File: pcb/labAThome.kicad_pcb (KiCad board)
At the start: 2 copper layers, 100 x 100 mm, 57 parts, among them J1 BME280, J10 SRV2, J12 FA2, J13 Barrel_Jack_Switch, J14 FA3, J2 SRV1, J3 5V, J4 EXTENSION, J5 VPS, J9 FA1, K1 G5V-2, K2 G5V-2, K3 G5V-2, Q2 IRLZ44N, Q3 IRLZ44N, Q4 BC547, SW1 RED, SW2 GREEN, SW3 YELLOW, SW4 BLUE, SW5 WHITE, SW6 FAN, U1 HC-SR501, U2 24V->5V, U3 PDC004_Module, U4 ESP32_DEVKITC_COMPATIBLE, U5 LD06AJSA, U6 GY-302, U7 Display, U8 INMP441_Module

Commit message: SchematicsV3 as ordered at JLCPCB
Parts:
- removed D1: RED, LED_THT:LED_D5.0mm
- removed D2: GREEN, LED_THT:LED_D5.0mm
- removed D3: YELLOW, LED_THT:LED_D5.0mm
- removed J14: FA3, Connector:FanPinHeader_1x03_P2.54mm_Vertical
- added C1: CP, Capacitor_THT:CP_Radial_Tantal_D5.0mm_P5.00mm, F.Cu at (72.1, 61.7)
- added D5: 1N4001, Diode_THT:D_DO-41_SOD81_P7.62mm_Horizontal, B.Cu at (73.7, 64.5)
- added J11: 1wire, Connector_JST:JST_PH_B3B-PH-K_1x03_P2.00mm_Vertical, B.Cu at (41.7, 101.2)
- added J6: FAN3, Connector:FanPinHeader_1x03_P2.54mm_Vertical, B.Cu at (48.5, 64.5)
- added J7: 1wire, Connector_JST:JST_PH_B3B-PH-K_1x03_P2.00mm_Vertical, B.Cu at (41.6, 87.1)
- added J8: 1wire, Connector_JST:JST_PH_B3B-PH-K_1x03_P2.00mm_Vertical, B.Cu at (47.4, 81.4)
- added JP4: 5V FAN1+2 24V, Connector_PinSocket_2.54mm:PinSocket_1x03_P2.54mm_Vertical, F.Cu at (43.3, 60.2)
- added Q1: IRLZ44N, Package_TO_SOT_THT:TO-220-3_Horizontal_TabDown, B.Cu at (58.3, 90.8)
- added U10: MAX3485_MODULE, smopla:MAX3485_MODULE, B.Cu at (99.1, 116.3)
- added U11: AM312, smopla:AM312, F.Cu at (80.0, 59.6)
- added U9: NEOPIXEL_STICK, smopla:NEOPIXEL_STICK, F.Cu at (47.9, 38.5)
- added X1: FAN_6024, smopla:FAN_6024, B.Cu at (74.5, 110.2)
- BZ1: footprint Buzzer_Beeper:Buzzer_12x9.5RM7.6 -> smopla:Buzzer_12x9.5RM6.6
- D8: footprint Diode_THT:D_DO-35_SOD27_P7.62mm_Horizontal -> Diode_THT:D_DO-35_SOD27_P2.54mm_Vertical_AnodeUp
- J1: footprint Connector_PinHeader_2.54mm:PinHeader_1x06_P2.54mm_Vertical -> Connector_PinHeader_2.54mm:PinHeader_1x04_P2.54mm_Vertical; moved to F.Cu
- J12: value FA2 -> FAN2
- J3: footprint Connector_PinHeader_2.54mm:PinHeader_1x05_P2.54mm_Vertical -> Connector_PinHeader_2.54mm:PinHeader_1x04_P2.54mm_Vertical
- J9: value FA1 -> FAN1
- JP3: value 3V3_5V -> R3_BUZZ; footprint Jumper:SolderJumper-3_P2.0mm_Open_TrianglePad1.0x1.5mm_NumberLabels -> Connector_PinSocket_2.54mm:PinSocket_1x03_P2.54mm_Vertical
- Q4: footprint Package_TO_SOT_THT:TO-92_Inline -> Package_TO_SOT_THT:TO-92_HandSolder
- R1, R13, R14, R15, R16, R2, R6: footprint Resistor_THT:R_Axial_DIN0207_L6.3mm_D2.5mm_P7.62mm_Horizontal -> Resistor_THT:R_Axial_DIN0207_L6.3mm_D2.5mm_P2.54mm_Vertical
- R3, R5: value 68R -> 1K; footprint Resistor_THT:R_Axial_DIN0207_L6.3mm_D2.5mm_P7.62mm_Horizontal -> Resistor_THT:R_Axial_DIN0207_L6.3mm_D2.5mm_P2.54mm_Vertical
- R4: value 68R -> 10K; footprint Resistor_THT:R_Axial_DIN0207_L6.3mm_D2.5mm_P7.62mm_Horizontal -> Resistor_THT:R_Axial_DIN0207_L6.3mm_D2.5mm_P2.54mm_Vertical
- SW6: value FAN -> FAN2; footprint smopla:MTS-102 -> smopla:SS12D00
- U1: value HC-SR501 -> SR602; footprint smopla:HC-SR501 -> smopla:SR602
- moved R1 68.4 mm to (47.5, 86.9), turned to 90 degrees
- moved JP3 46.0 mm to (96.5, 103.4)
- moved R2 45.8 mm to (50.5, 86.9)
- moved R10 34.9 mm to (118.6, 60.5), turned to 180 degrees
- moved U5 34.2 mm to (50.8, 112.4), turned to 180 degrees
- moved R14 21.2 mm to (123.7, 124.7), turned to 180 degrees
- moved R12 20.4 mm to (91.9, 81.5), turned to 90 degrees
- moved Q4 18.7 mm to (95.5, 78.5)
- moved R5 18.3 mm to (47.4, 76.6), turned to 0 degrees
- moved R3 14.2 mm to (50.5, 92.2), turned to 90 degrees
- moved RV1 13.4 mm to (39.6, 70.0)
- moved R15 12.2 mm to (50.4, 106.4)
- moved R16 12.2 mm to (47.4, 106.4)
- moved J12 8.84 mm to (34.7, 65.3)
- moved R13 8.66 mm to (103.1, 110.5), turned to 180 degrees
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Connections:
- J10 pad 1: I2S_SD -> 1wire
- J2 pad 1: I2S_SCK -> SERVO_PWM1
- J9 pad 2: +5V -> Net-(J6-Pad2)
- JP3 pad 1: +3V3 -> R3_ON
- JP3 pad 3: +5V -> BUZZER
- R11 pad 1: /Q2_D -> +24V
- R11 pad 2: +24V -> /Q2_D
- R3 pad 1: +3V3 -> 1wire
- R3 pad 2: Net-(D1-Pad2) -> Net-(Q1-Pad1)
- R4 pad 1: +3V3 -> GND
- R4 pad 2: Net-(D2-Pad2) -> Net-(Q1-Pad1)
- R5 pad 2: Net-(D3-Pad2) -> 1wire
- U1 pad 1: Net-(JP3-Pad2) -> +3V3
- U1 pad 2: MOVEMENT -> GND
- U1 pad 3: GND -> MOVEMENT
- U4 pad 10: LED_RED -> LED_STRIP
- U4 pad 11: LED_YELLOW -> 1wire
- U4 pad 12: LED_POWER_WHITE -> I2S_SCK
- U4 pad 15: LED_GREEN -> LED_POWER_WHITE
- U4 pad 24: LCD_BL -> HEATER
- U4 pad 26: I2S_SD -> I2S_WS
- U4 pad 27: HEATER -> I2S_SD
- U4 pad 28: R3_ON -> Net-(JP3-Pad2)
- U4 pad 29: BUZZER -> LCD_DC
- U4 pad 31: LCD_DC -> LCD_RES
- U4 pad 9: I2S_SCK -> SERVO_PWM1
- U7 pad 5: +3V3 -> LCD_RES
- U7 pad 7: LCD_BL -> Net-(U7-Pad7)
- U8 pad 2: HEATER -> I2S_WS
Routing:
- net Net-(J5-Pad1): track 6.22 -> 108.9 mm, vias 0 -> 3
- net LED_STRIP: track 0.00 -> 94.1 mm
- net I2S_SD: track 113.4 -> 19.6 mm, vias 1 -> 0
- net 1wire: track 0.00 -> 93.6 mm, vias 0 -> 1
- net R3_A1: track 74.1 -> 9.43 mm, vias 1 -> 0
- net LED_POWER_WHITE: track 61.3 -> 4.07 mm, vias 1 -> 0
- net SERVO_PWM1: track 0.00 -> 55.0 mm
- net I2S_SCK: track 103.1 -> 48.3 mm, vias 1 -> 7
- net GND: track 89.4 -> 142.1 mm, vias 19 -> 201
- net LCD_BL: track 43.9 -> 0.00 mm
- net Net-(D5-Pad1): track 0.00 -> 37.2 mm
- net R3_12: track 42.5 -> 12.6 mm
- net /FAN_SWITCH2: track 0.00 -> 27.8 mm
- net I2S_WS: track 0.00 -> 25.2 mm
- net Net-(D2-Pad2): track 22.6 -> 0.00 mm
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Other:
- board text added: "-"
- board text added: "EXT"
- board text added: "Gegenseitiger Ausschluss: - 1wire und Servo2 - I2S und RS485 - Relay 3 und Buzzer"
- board text removed: "EXTENSION CONNECTOR"

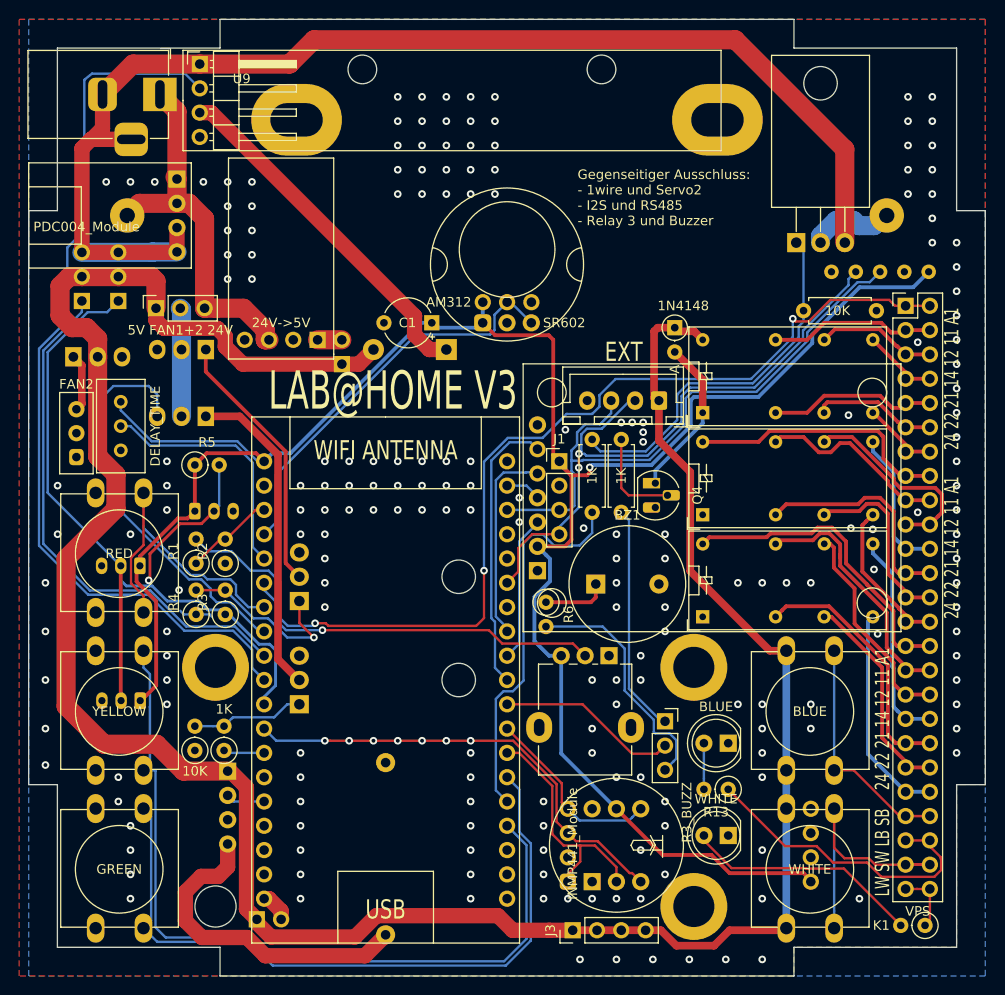
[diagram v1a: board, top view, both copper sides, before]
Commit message: PCB  V4 as ordered at JLCPCB
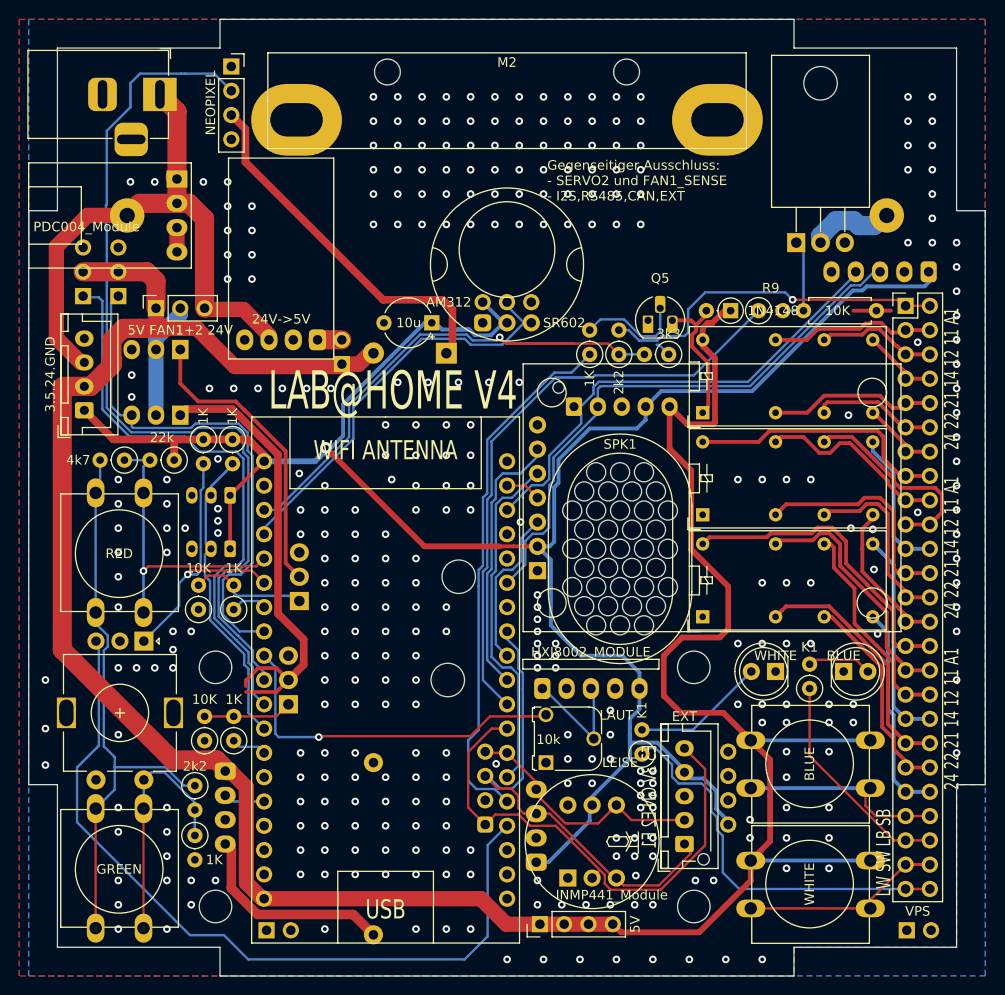
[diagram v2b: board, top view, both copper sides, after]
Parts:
- removed BZ1: Buzzer, smopla:Buzzer_12x9.5RM6.6
- removed Q4: BC547, Package_TO_SOT_THT:TO-92_HandSolder
- removed R6: K1, Resistor_THT:R_Axial_DIN0207_L6.3mm_D2.5mm_P2.54mm_Vertical
- removed RV2: R_POT, Potentiometer_THT:Potentiometer_Alpha_RD901F-40-00D_Single_Vertical
- removed SW3: YELLOW, Button_Switch_THT:SW_PUSH-12mm
- removed SW6: FAN2, smopla:SS12D00
- removed U9: NEOPIXEL_STICK, smopla:NEOPIXEL_STICK
- added M1: HXJ8002_MODULE, smopla:HXJ8002_MODULE_VERTICAL, F.Cu at (83.7, 99.9)
- added M2: NEOPIXEL, smopla:NEOPIXEL_STICK, F.Cu at (80.0, 35.5)
- added M3: SN65HVD230_MODULE, smopla:SN65HVD230_MODULE, B.Cu at (83.1, 114.3)
- added Q5: 2N3904, Package_TO_SOT_THT:TO-92_HandSolder, F.Cu at (94.7, 61.5)
- added R18: 22k, Resistor_THT:R_Axial_DIN0207_L6.3mm_D2.5mm_P2.54mm_Vertical, F.Cu at (45.2, 76.1)
- added R19: 4k7, Resistor_THT:R_Axial_DIN0207_L6.3mm_D2.5mm_P2.54mm_Vertical, F.Cu at (40.0, 76.1)
- added R20: 2k2, Resistor_THT:R_Axial_DIN0207_L6.3mm_D2.5mm_P2.54mm_Vertical, F.Cu at (47.4, 110.1)
- added R21: 1K, Resistor_THT:R_Axial_DIN0207_L6.3mm_D2.5mm_P2.54mm_Vertical, F.Cu at (47.4, 115.3)
- added R7: 1K, Resistor_THT:R_Axial_DIN0207_L6.3mm_D2.5mm_P2.54mm_Vertical, F.Cu at (48.3, 73.9)
- added SPK1: SPEAKER, smopla:SPEAKER_2415, F.Cu at (91.8, 85.3)
- added SW7: ROTENC, smopla:RotaryEncoder_Alps_EC11E-Switch_Vertical_H20mm, F.Cu at (42.0, 95.0)
- C1: value CP -> 10u
- J1: value BME280 -> I2C; footprint Connector_PinHeader_2.54mm:PinHeader_1x04_P2.54mm_Vertical -> Connector_JST:JST_XH_B5B-XH-AM_1x05_P2.50mm_Vertical; moved to B.Cu
- J11: value 1wire -> 3.5.24.GND; footprint Connector_JST:JST_PH_B3B-PH-K_1x03_P2.00mm_Vertical -> Connector_JST:JST_XH_B4B-XH-A_1x04_P2.50mm_Vertical; moved to F.Cu
- J12: value FAN2 -> NEOPIXEL; footprint Connector:FanPinHeader_1x03_P2.54mm_Vertical -> Connector_PinSocket_2.54mm:PinSocket_1x04_P2.54mm_Vertical; moved to F.Cu
- J4: value EXTENSION -> EXT; footprint Connector_JST:JST_XH_B4B-XH-A_1x04_P2.50mm_Vertical -> Connector_JST:JST_XH_B5B-XH-AM_1x05_P2.50mm_Vertical
- JP2: value 5V_ESP -> MECHANICAL
- JP3: value R3_BUZZ -> MECHANICAL; footprint Connector_PinSocket_2.54mm:PinSocket_1x03_P2.54mm_Vertical -> Connector_PinHeader_2.54mm:PinHeader_1x02_P2.54mm_Vertical; moved to B.Cu
- R12, R9: footprint Resistor_THT:R_Axial_DIN0207_L6.3mm_D2.5mm_P7.62mm_Horizontal -> Resistor_THT:R_Axial_DIN0207_L6.3mm_D2.5mm_P2.54mm_Vertical
- RV1: value DELAY_TIME -> 10k; footprint Potentiometer_THT:Potentiometer_Bourns_3296W_Vertical -> Potentiometer_THT:Potentiometer_Runtron_RM-065_Vertical
- moved RV1 58.3 mm to (84.1, 107.7)
- moved R2 51.2 mm to (96.9, 65.0), turned to 180 degrees
- moved R1 49.3 mm to (91.7, 65.0)
- moved J4 46.4 mm to (98.6, 116.2), turned to 90 degrees
- moved R14 34.6 mm to (94.1, 106.8), turned to 90 degrees
- moved J12 34.6 mm to (51.2, 34.9)
- moved JP3 33.4 mm to (121.8, 125.2), turned to 270 degrees
- moved J11 30.9 mm to (35.8, 70.9), turned to 90 degrees
- moved R9 27.3 mm to (106.3, 60.5), turned to 0 degrees
- moved D7 17.8 mm to (108.1, 98.2)
- moved R12 16.8 mm to (88.6, 65.0)
- moved SW4 14.9 mm to (118.0, 110.4), turned to 180 degrees
- moved D6 14.2 mm to (115.2, 98.2), turned to 0 degrees
- moved R13 13.5 mm to (111.6, 99.9), turned to 90 degrees
- moved SW5 11.1 mm to (118.0, 122.9), turned to 180 degrees
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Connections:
- net FAN_DRIVE renamed FAN1_DRIVE
- net Net-(J5-Pad1) renamed /R3_INPUT
- J1 pad 1: +3V3 -> SDA
- J1 pad 2: GND -> SCL
- J1 pad 3: SCL -> GND
- J1 pad 4: SDA -> +3V3
- J10 pad 1: 1wire -> FAN1_SENSE
- J11 pad 2: 1wire -> +5V
- J11 pad 3: GND -> +24V
- J12 pad 1: Net-(J12-Pad1) -> GND
- J12 pad 2: +5V -> LED_STRIP
- J12 pad 3: Net-(J12-Pad3) -> Net-(D5-Pad1)
- J2 pad 1: SERVO_PWM1 -> SERVO1
- J4 pad 1: +5V -> 485_DE
- J4 pad 2: SDA -> 485_DI
- J4 pad 3: SCL -> GND
- J4 pad 4: GND -> +3V3
- J9 pad 3: FAN_SENSE -> FAN1_SENSE
- JP2 pad 1: +5V -> GND
- JP2 pad 2: Net-(JP2-Pad2) -> GND
- JP3 pad 1: R3_ON -> GND
- JP3 pad 2: Net-(JP3-Pad2) -> GND
- R3 pad 1: 1wire -> FAN2_DRIVE
- RV1 pad 1: +3V3 -> GND
- RV1 pad 2: POTI_T -> Net-(M1-Pad1)
- RV1 pad 3: GND -> SPEAKER
- SW1 pad 1: SW_RED -> SW
- SW1 pad 2: GND -> Net-(R19-Pad2)
- SW2 pad 1: SW_GREEN -> Net-(R20-Pad2)
- SW2 pad 2: GND -> Net-(R19-Pad2)
- U1 pad 1: +3V3 -> GND
- U1 pad 2: GND -> +3V3
- U10 pad 1: I2S_WS -> 485_RO
- U10 pad 3: I2S_SCK -> 485_DE
- U10 pad 4: I2S_SD -> 485_DI
- U4 pad 11: 1wire -> SERVO1
- U4 pad 12: I2S_SCK -> 1wire
- U4 pad 19: Net-(JP2-Pad2) -> +5V
- U4 pad 23: SW_YELLOW -> ROTENC_B
- U4 pad 24: HEATER -> R3_ON
- U4 pad 25: SW_GREEN -> LCD_RES
- U4 pad 26: I2S_WS -> 485_DI
- U4 pad 27: I2S_SD -> 485_RO
- U4 pad 28: Net-(JP3-Pad2) -> HEATER
- U4 pad 31: LCD_RES -> 485_DE
- U4 pad 33: SDA -> SCL
- U4 pad 36: SCL -> SDA
- U4 pad 5: POTI_T -> SW
- U4 pad 6: POTI -> ROTENC_A
- U4 pad 7: SW_RED -> FAN2_DRIVE
- U4 pad 8: FAN_SENSE -> FAN1_SENSE
- U4 pad 9: SERVO_PWM1 -> SPEAKER
- U8 pad 2: I2S_WS -> 485_RO
- U8 pad 3: I2S_SCK -> 485_DE
- U8 pad 4: I2S_SD -> 485_DI
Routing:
- net GND: track 142.1 -> 8.16 mm, vias 201 -> 350
- net SW_YELLOW: track 84.6 -> 0.00 mm
- net ROTENC_B: track 0.00 -> 82.3 mm
- net SW_GREEN: track 74.5 -> 0.00 mm
- net /R3_INPUT: track 108.9 -> 37.0 mm, vias 3 -> 1
- net 1wire: track 93.6 -> 32.2 mm, vias 1 -> 0
- net Net-(R19-Pad2): track 0.00 -> 60.3 mm
- net SERVO1: track 0.00 -> 60.2 mm
- net SERVO_PWM1: track 55.0 -> 0.00 mm
- net 485_RO: track 0.00 -> 54.7 mm
- net FAN1_SENSE: track 0.00 -> 54.6 mm
- net 485_DE: track 0.00 -> 50.5 mm
- net I2S_SCK: track 48.3 -> 0.00 mm, vias 7 -> 0
- net R3_A1: track 9.43 -> 57.4 mm, vias 0 -> 1
- net FAN_SENSE: track 42.9 -> 0.00 mm
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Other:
- board text added: "- + Sense"
- board text added: "5V"
- board text added: "5V 3V3 GND SCL SDA"
- board text added: "E3 3V GN E2 E1"
- board text added: "Für Lehre und Forschung Klaus Liebler, 2020-08-11 Westfälische Hochschule"
- board text added: "GND"
- board text added: "Gegenseitiger Ausschluss: - SERVO2 und FAN1_SENSE - I2S,RS485,CAN,EXT"
- board text added: "LAB@HOME V4"
- board text added: "LAUT"
- board text added: "LEISE"
- board text added: "PWM"
- board text removed: "EXT"
- board text removed: "Für Lehre und Forschung! Klaus Liebler, 2020-06-17 Westfälische Hochschule"
- board text removed: "Gegenseitiger Ausschluss: - 1wire und Servo2 - I2S und RS485 - Relay 3 und Buzzer"
- board text removed: "LAB@HOME V3"

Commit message: PCB last version without SMD
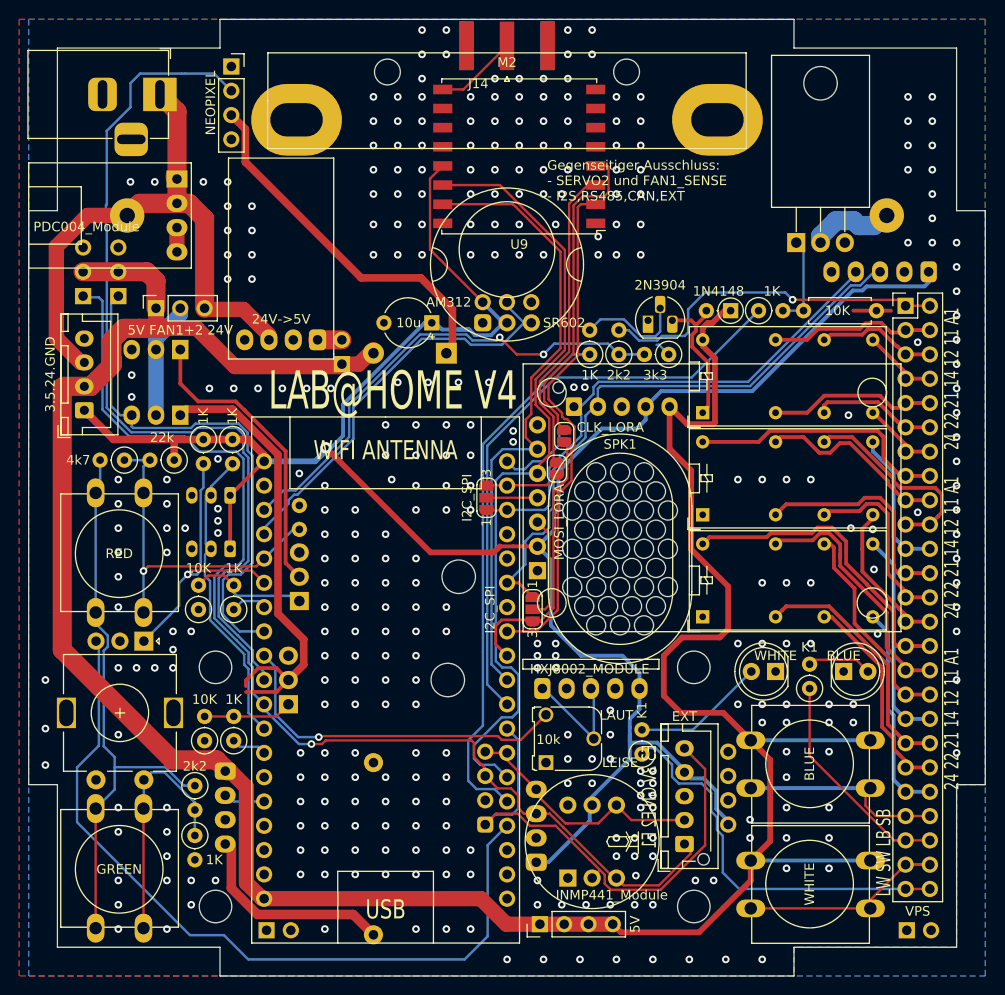
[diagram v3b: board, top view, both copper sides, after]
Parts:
- added C2: u1, Capacitor_THT:C_Rect_L4.0mm_W2.5mm_P2.50mm, B.Cu at (58.3, 83.3)
- added J14: Conn_Coaxial, Connector_Coaxial:SMA_Amphenol_132289_EdgeMount, F.Cu at (80.0, 32.8)
- added JP5: CLK_LORA, Jumper:SolderJumper-2_P1.3mm_Open_RoundedPad1.0x1.5mm, F.Cu at (86.0, 73.5)
- added JP6: MOSI_LORA, Jumper:SolderJumper-2_P1.3mm_Open_RoundedPad1.0x1.5mm, F.Cu at (85.2, 77.0)
- added JP8: I2C_SPI, Jumper:SolderJumper-3_P1.3mm_Open_RoundedPad1.0x1.5mm_NumberLabels, F.Cu at (82.7, 91.7)
- added JP9: I2C_SPI, Jumper:SolderJumper-3_P1.3mm_Open_RoundedPad1.0x1.5mm_NumberLabels, F.Cu at (77.9, 80.0)
- added U9: RFM95W-868S2, RF_Module:HOPERF_RFM9XW_SMD, F.Cu at (81.3, 44.3)
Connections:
- net LCD_DC renamed SPI_IO1
- net LCD_RES renamed SPI_IO2
- J2 pad 1: SERVO1 -> 485_DE
- U4 pad 11: SERVO1 -> 485_DE
- U4 pad 30: LCD_CLK -> SPI_CLK
- U4 pad 31: 485_DE -> SPI_MISO
- U4 pad 37: LCD_MOSI -> SPI_MOSI
- U7 pad 3: LCD_CLK -> Net-(JP8-Pad2)
- U7 pad 4: LCD_MOSI -> Net-(JP9-Pad2)
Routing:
- net 485_DE: track 50.5 -> 118.0 mm, vias 0 -> 1
- net SERVO1: track 60.2 -> 0.00 mm
- net SPI_MISO: track 0.00 -> 53.6 mm
- net SPI_IO2: track 36.6 -> 83.4 mm
- net SPI_IO1: track 28.3 -> 66.6 mm
- net Net-(JP5-Pad2): track 0.00 -> 33.8 mm
- net Net-(JP6-Pad2): track 0.00 -> 32.6 mm
- net SPI_CLK: track 0.00 -> 28.7 mm
- net LCD_CLK: track 16.8 -> 0.00 mm
- net +3V3: track 220.6 -> 236.7 mm
- net Net-(JP8-Pad2): track 0.00 -> 11.1 mm
- net GND: track 8.16 -> 16.8 mm, vias 350 -> 356
- net Net-(J14-Pad1): track 0.00 -> 8.61 mm
- net SPI_MOSI: track 0.00 -> 7.85 mm
- net R3_A1: track 57.4 -> 51.3 mm, vias 1 -> 2
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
